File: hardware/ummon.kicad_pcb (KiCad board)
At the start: 4 copper layers, 60 x 60 mm, 95 parts, among them J1 Conn_01x08_Pin, J2 Conn_01x05_Pin, J3 Conn_01x04_Pin, J4 Conn_01x04_Pin, J5 Conn_01x04_Pin, P1 FPC 0.5MM 24P Vertical, Q1 SI1308EDL, SW1 Reboot, SW2 Flash, SW3 Test Button, U1 ESP32-C6-WROOM-1-N8, U2 SCD41-D-R2, U3 SGP41-D-R4, U4 SHT41-AD1B-R2, U5 AMS1117-3.3

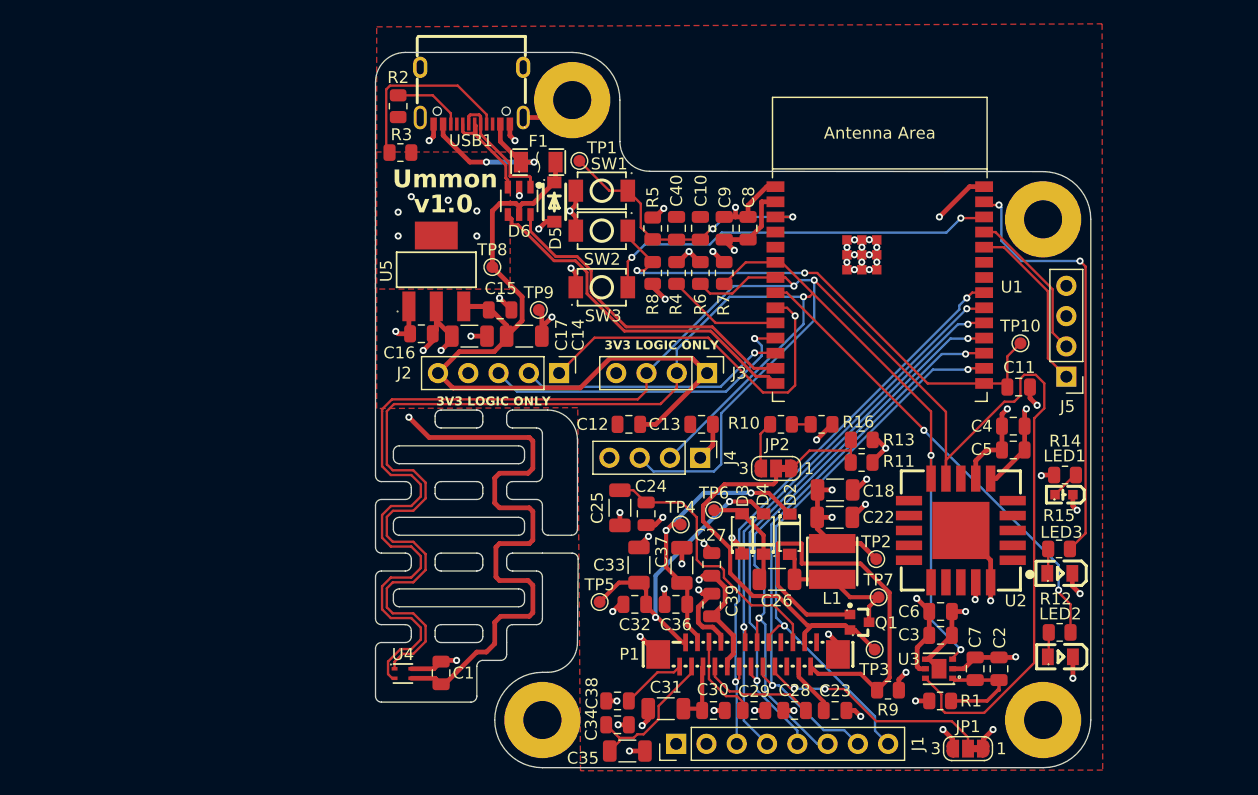
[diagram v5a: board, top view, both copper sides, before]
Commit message: :recycle: Replace RSE solder jumper with MSK12CO2 slide switch
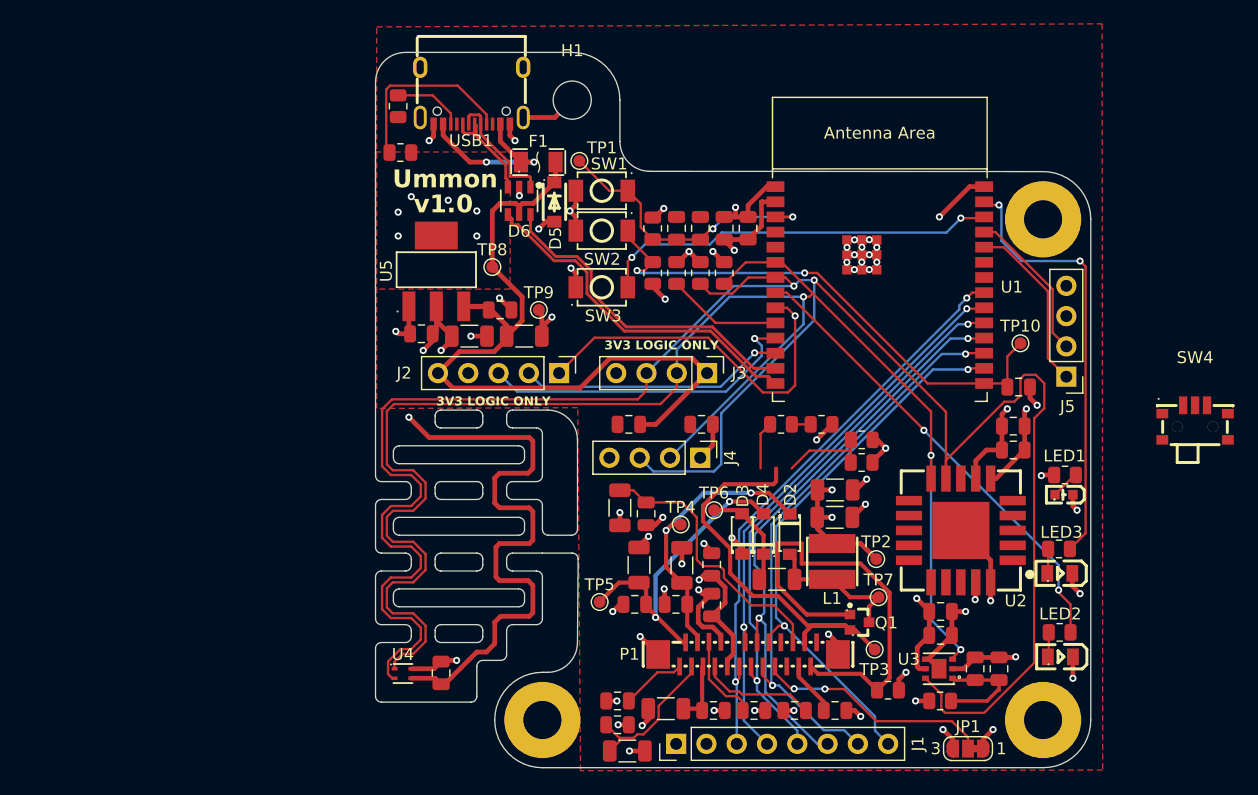
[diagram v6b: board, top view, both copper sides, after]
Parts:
- removed JP2: RSE_Jumper, Jumper:SolderJumper-3_P1.3mm_Bridged12_RoundedPad1.0x1.5mm_NumberLabels
- added SW4: MINI MSK12CO2, parts:SW-SMD_MSK12CO2, F.Cu at (183.8, 121.0)
- H1: value MountingHole_Pad -> MountingHole; footprint MountingHole:MountingHole_3.2mm_M3_Pad -> MountingHole:MountingHole_3.2mm_M3

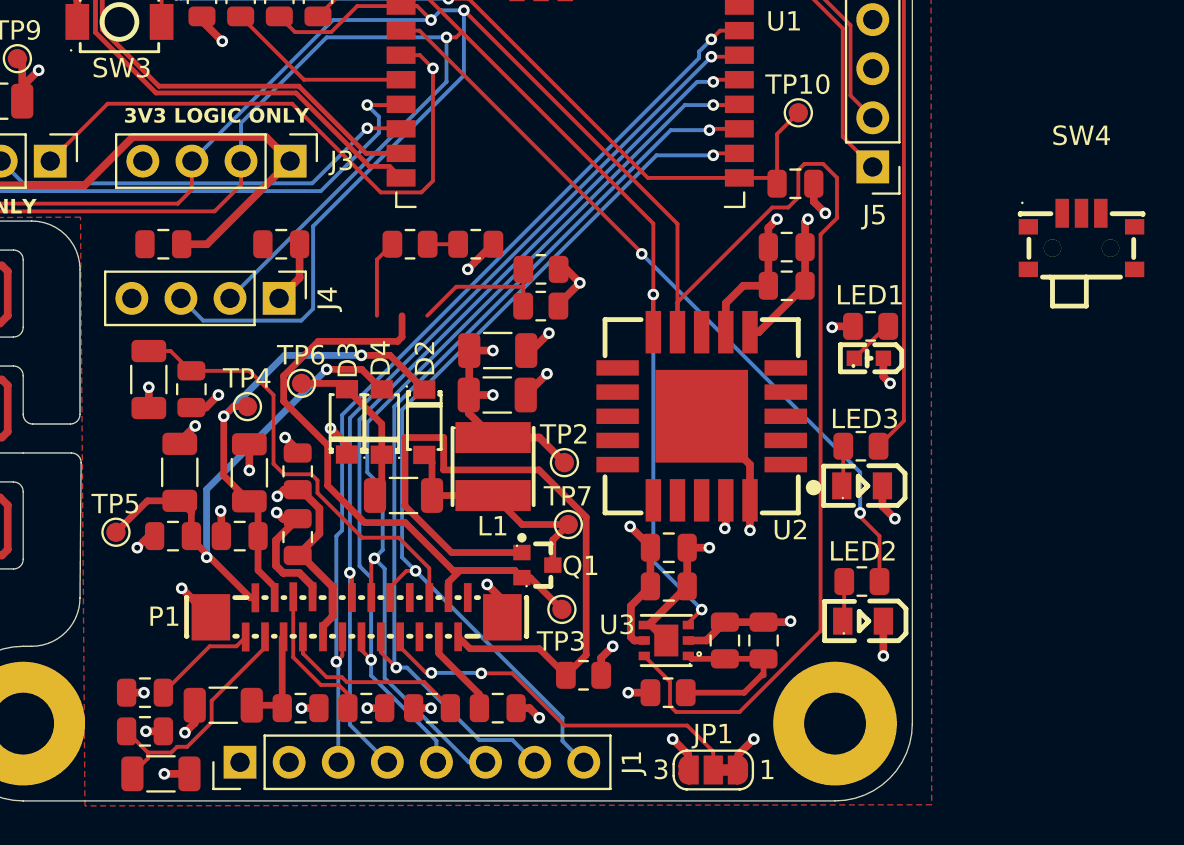
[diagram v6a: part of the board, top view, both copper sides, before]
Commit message: :construction: Place slide switch and rearrange RESE resistors
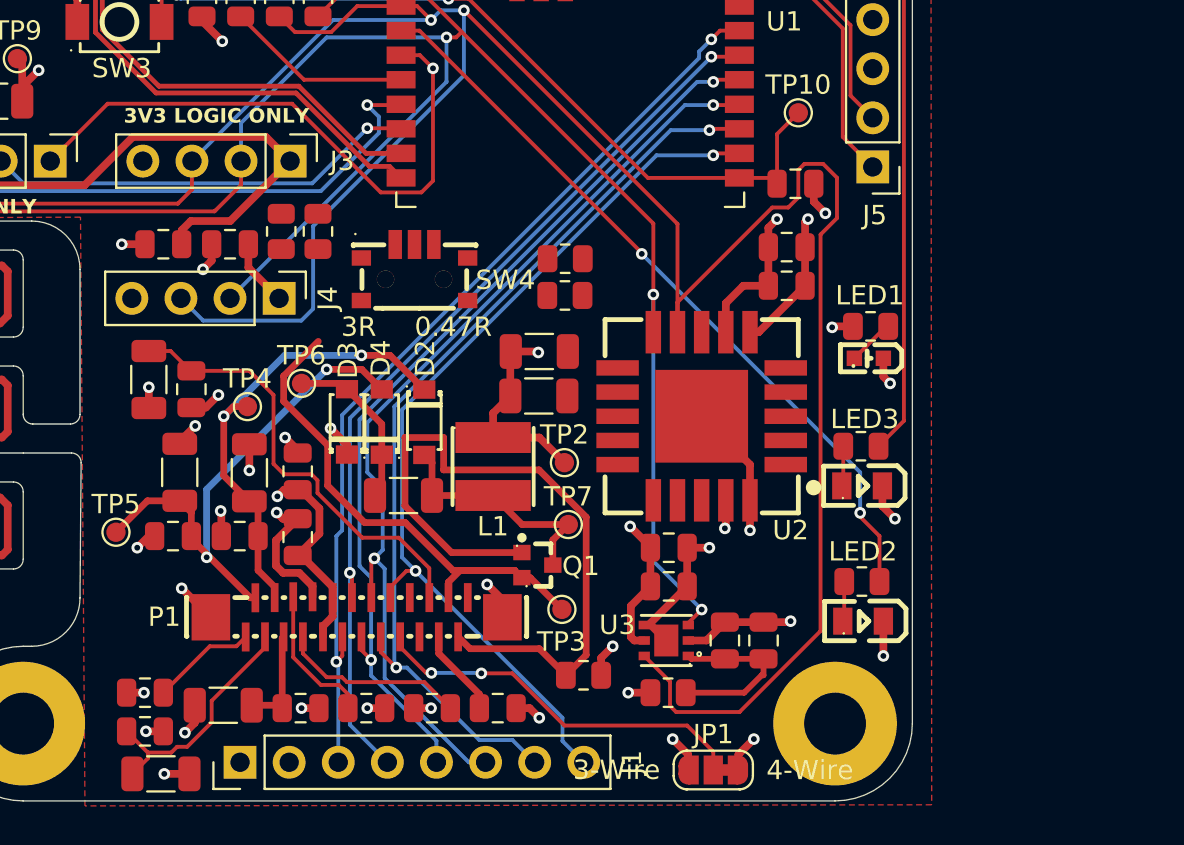
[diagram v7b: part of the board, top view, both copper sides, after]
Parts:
- moved SW4 34.5 mm to (149.2, 122.7)
- moved R16 10.1 mm to (142.3, 120.5), turned to 90 degrees
- moved R10 4.81 mm to (144.2, 120.5), turned to -90 degrees
- moved C13 2.65 mm to (139.7, 121.2)
- moved C22 2.15 mm to (155.7, 129.1)
- moved C18 2.15 mm to (155.7, 126.8)
- moved R11 1.37 mm to (157.0, 123.8)
- moved R13 1.37 mm to (157.0, 122.0)
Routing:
- net Net-(R11-Pad2): track 7.50 -> 0.00 mm
- net /EPD_RESE: track 33.9 -> 28.4 mm
- net GND: track 162.5 -> 157.2 mm, vias 58 -> 56
- net Net-(R10-Pad2): track 4.03 -> 0.00 mm
- net Net-(R10-Pad1): track 1.57 -> 0.00 mm
- net +3.3V: track 124.5 -> 123.5 mm, vias 23 -> 22

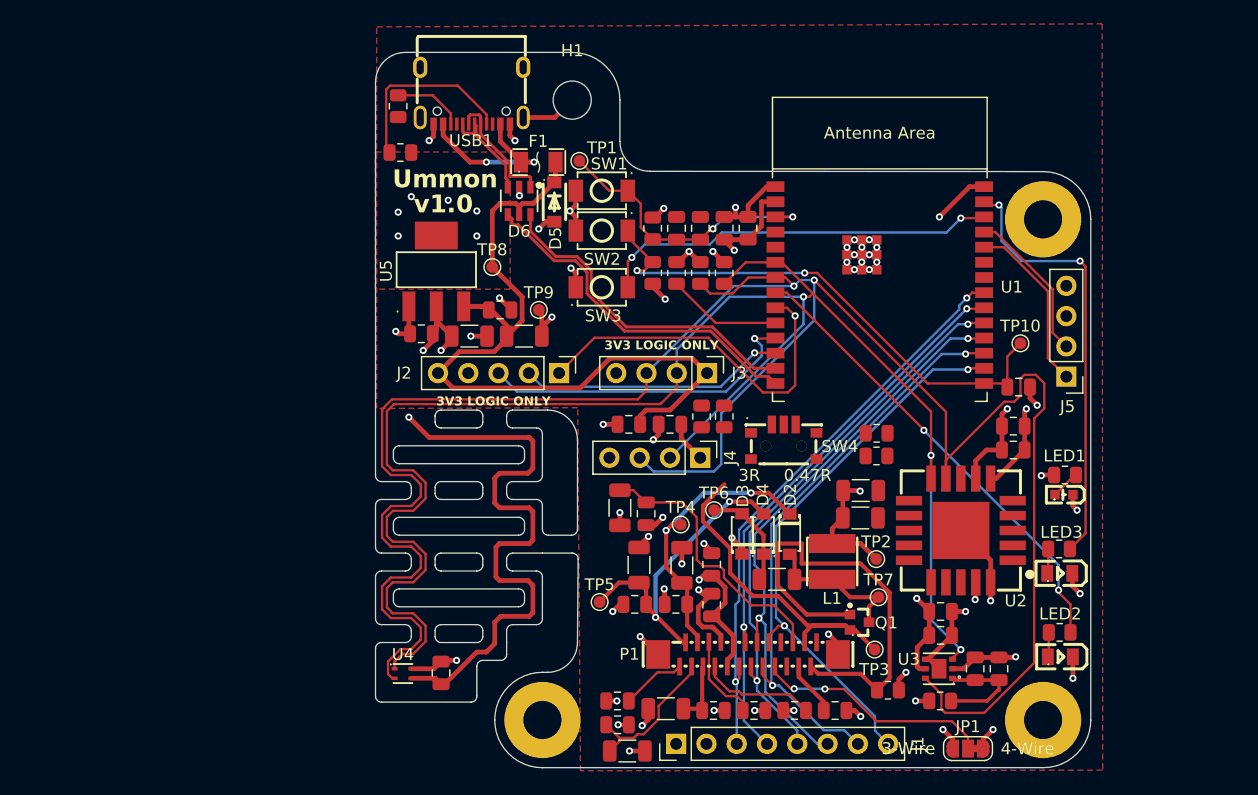
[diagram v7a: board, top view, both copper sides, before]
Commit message: :recycle: Name testpoints and move part of 3V3 to inner layer
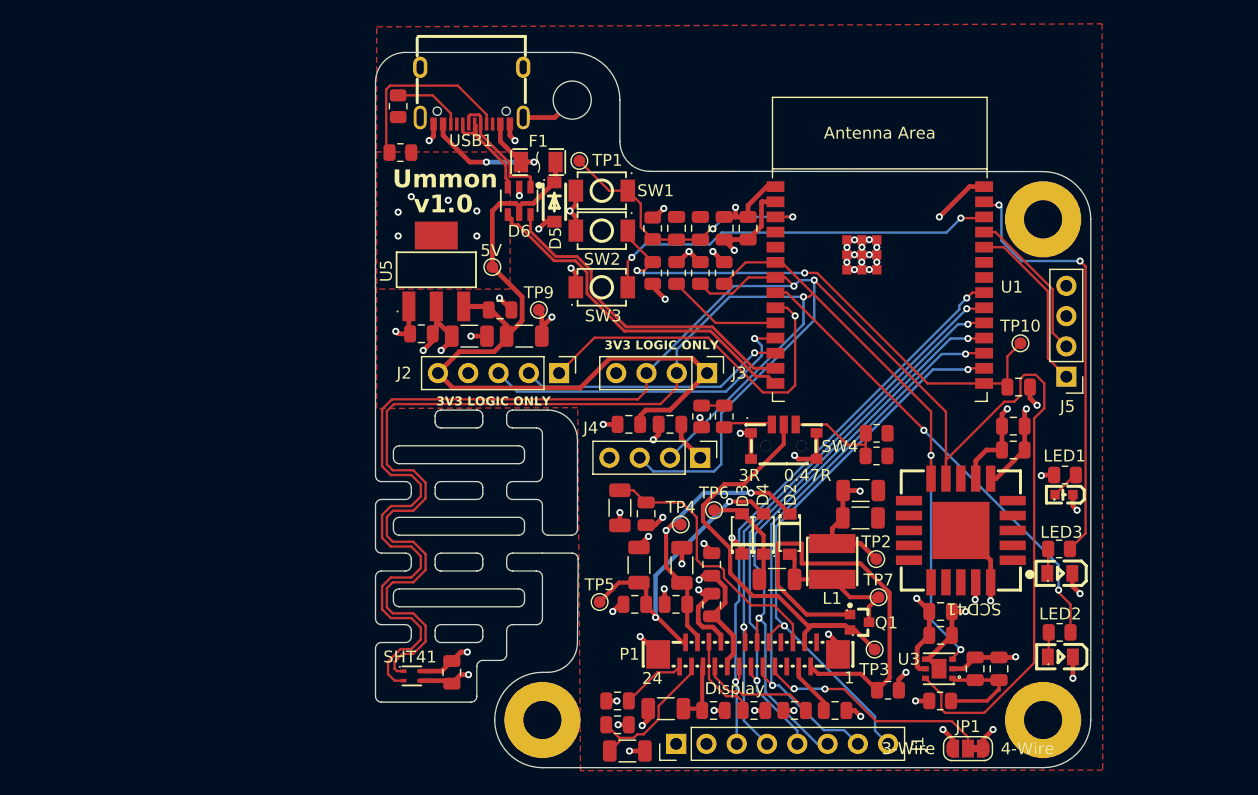
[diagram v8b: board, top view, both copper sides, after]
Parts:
- P1: value FPC 0.5MM 24P Vertical -> Display
- TP1: value TestPoint -> EN
- TP10: value TestPoint -> GPIO9
- TP2: value TestPoint -> 3V3
- TP3: value TestPoint -> RESE
- TP4: value TestPoint -> PVGH
- TP5: value TestPoint -> PVGL
- TP6: value TestPoint -> VGL
- TP7: value TestPoint -> VGH
- TP8: value TestPoint -> 5V
- TP9: value TestPoint -> GND
- U2: value SCD41-D-R2 -> SCD41
- U3: value SGP41-D-R4 -> SGP41
- U4: value SHT41-AD1B-R2 -> SHT41
- moved C1 0.90 mm to (121.4, 142.0)
- moved U4 0.78 mm to (118.0, 142.3)
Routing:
- net Net-(R11-Pad2): track 0.00 -> 8.48 mm
- net /EPD_RESE: track 28.4 -> 36.4 mm
- net GND: track 157.2 -> 164.6 mm, vias 56 -> 59
- net Net-(R10-Pad2): track 0.00 -> 4.19 mm
- net Net-(R10-Pad1): track 0.00 -> 1.90 mm
- net /I2C_SCL: track 184.9 -> 185.7 mm
- net +3.3V: track 123.5 -> 122.7 mm
- net /I2C_SDA: track 142.2 -> 143.0 mm
